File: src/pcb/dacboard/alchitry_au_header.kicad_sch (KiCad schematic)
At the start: 0 parts

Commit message: dacboard routing
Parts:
- added J14, J15, J17, J18, J19, J20, J21, J4, J6: Conn_01x14, Connector_PinHeader_2.54mm:PinHeader_1x14_P2.54mm_Vertical, symbol Connector_Generic:Conn_01x14
- added J22: Conn_01x06, Connector_PinHeader_2.54mm:PinHeader_1x06_P2.54mm_Vertical, symbol Connector_Generic:Conn_01x06
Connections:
- new net AUX_IO1: J20.9 (Pin_9), J22.1 (Pin_1)
- new net AUX_IO2: J20.10 (Pin_10), J22.2 (Pin_2)
- new net AUX_IO3: J20.11 (Pin_11), J22.3 (Pin_3)
- new net AUX_IO4: J20.12 (Pin_12), J22.4 (Pin_4)
- new net AUX_IO5: J20.13 (Pin_13), J22.5 (Pin_5)
- new net AUX_IO6: J20.14 (Pin_14), J22.6 (Pin_6)
- new net CS_N_CH1: J4.4 (Pin_4)
- new net CS_N_CH10: J14.14 (Pin_14)
- new net CS_N_CH11: J15.5 (Pin_5)
- new net CS_N_CH12: J15.9 (Pin_9)
- new net CS_N_CH13: J15.13 (Pin_13)
- new net CS_N_CH14: J17.4 (Pin_4)
- new net CS_N_CH15: J17.8 (Pin_8)
- new net CS_N_CH16: J17.13 (Pin_13)
- new net CS_N_CH17: J18.4 (Pin_4)
- new net CS_N_CH18: J18.8 (Pin_8)
- new net CS_N_CH19: J18.13 (Pin_13)
- new net CS_N_CH2: J4.8 (Pin_8)
- new net CS_N_CH20: J19.4 (Pin_4)
- new net CS_N_CH21: J19.8 (Pin_8)
- new net CS_N_CH22: J19.12 (Pin_12)
- new net CS_N_CH23: J20.3 (Pin_3)
- new net CS_N_CH24: J20.7 (Pin_7)
- new net CS_N_CH3: J4.12 (Pin_12)
- new net CS_N_CH4: J6.3 (Pin_3)
- new net CS_N_CH5: J6.7 (Pin_7)
- new net CS_N_CH6: J6.11 (Pin_11)
- new net CS_N_CH7: J14.2 (Pin_2)
- new net CS_N_CH8: J14.6 (Pin_6)
- new net CS_N_CH9: J14.10 (Pin_10)
- new net LDAC_N_CH1: J4.5 (Pin_5)
- new net LDAC_N_CH10: J15.2 (Pin_2)
- new net LDAC_N_CH11: J15.6 (Pin_6)
- new net LDAC_N_CH12: J15.10 (Pin_10)
- new net LDAC_N_CH13: J15.14 (Pin_14)
- new net LDAC_N_CH14: J17.5 (Pin_5)
- new net LDAC_N_CH15: J17.10 (Pin_10)
- new net LDAC_N_CH16: J17.14 (Pin_14)
- new net LDAC_N_CH17: J18.5 (Pin_5)
- new net LDAC_N_CH18: J18.10 (Pin_10)
- new net LDAC_N_CH19: J18.14 (Pin_14)
- new net LDAC_N_CH2: J4.9 (Pin_9)
- new net LDAC_N_CH20: J19.5 (Pin_5)
- new net LDAC_N_CH21: J19.9 (Pin_9)
- new net LDAC_N_CH22: J19.13 (Pin_13)
- new net LDAC_N_CH23: J20.4 (Pin_4)
- new net LDAC_N_CH24: J20.8 (Pin_8)
- new net LDAC_N_CH3: J4.13 (Pin_13)
- new net LDAC_N_CH4: J6.4 (Pin_4)
- new net LDAC_N_CH5: J6.8 (Pin_8)
- new net LDAC_N_CH6: J6.12 (Pin_12)
- new net LDAC_N_CH7: J14.3 (Pin_3)
- new net LDAC_N_CH8: J14.7 (Pin_7)
- new net LDAC_N_CH9: J14.11 (Pin_11)
- new net MOSI_CH1: J4.3 (Pin_3)
- new net MOSI_CH10: J14.13 (Pin_13)
- new net MOSI_CH11: J15.4 (Pin_4)
- new net MOSI_CH12: J15.8 (Pin_8)
- new net MOSI_CH13: J15.12 (Pin_12)
- new net MOSI_CH14: J17.3 (Pin_3)
- new net MOSI_CH15: J17.7 (Pin_7)
- new net MOSI_CH16: J17.12 (Pin_12)
- new net MOSI_CH17: J18.3 (Pin_3)
- new net MOSI_CH18: J18.7 (Pin_7)
- new net MOSI_CH19: J18.12 (Pin_12)
- new net MOSI_CH2: J4.7 (Pin_7)
- new net MOSI_CH20: J19.3 (Pin_3)
- new net MOSI_CH21: J19.7 (Pin_7)
- new net MOSI_CH22: J19.11 (Pin_11)
- new net MOSI_CH23: J20.2 (Pin_2)
- new net MOSI_CH24: J20.6 (Pin_6)
- new net MOSI_CH3: J4.11 (Pin_11)
- new net MOSI_CH4: J6.2 (Pin_2)
- new net MOSI_CH5: J6.6 (Pin_6)
- new net MOSI_CH6: J6.10 (Pin_10)
- new net MOSI_CH7: J6.14 (Pin_14)
- new net MOSI_CH8: J14.5 (Pin_5)
- new net MOSI_CH9: J14.9 (Pin_9)
- new net NGND: J14.1 (Pin_1), J15.1 (Pin_1), J17.1 (Pin_1), J18.1 (Pin_1), J19.1 (Pin_1), J20.1 (Pin_1), J21.3 (Pin_3), J4.1 (Pin_1), J6.1 (Pin_1)
- new net SCLK_CH1: J4.2 (Pin_2)
- new net SCLK_CH10: J14.12 (Pin_12)
- new net SCLK_CH11: J15.3 (Pin_3)
- new net SCLK_CH12: J15.7 (Pin_7)
- new net SCLK_CH13: J15.11 (Pin_11)
- new net SCLK_CH14: J17.2 (Pin_2)
- new net SCLK_CH15: J17.6 (Pin_6)
- new net SCLK_CH16: J17.11 (Pin_11)
- new net SCLK_CH17: J18.2 (Pin_2)
- new net SCLK_CH18: J18.6 (Pin_6)
- new net SCLK_CH19: J18.11 (Pin_11)
- new net SCLK_CH2: J4.6 (Pin_6)
- new net SCLK_CH20: J19.2 (Pin_2)
- new net SCLK_CH21: J19.6 (Pin_6)
- new net SCLK_CH22: J19.10 (Pin_10)
- new net SCLK_CH23: J19.14 (Pin_14)
- new net SCLK_CH24: J20.5 (Pin_5)
- new net SCLK_CH3: J4.10 (Pin_10)
- new net SCLK_CH4: J4.14 (Pin_14)
- new net SCLK_CH5: J6.5 (Pin_5)
- new net SCLK_CH6: J6.9 (Pin_9)
- new net SCLK_CH7: J6.13 (Pin_13)
- new net SCLK_CH8: J14.4 (Pin_4)
- new net SCLK_CH9: J14.8 (Pin_8)
- new net VCCN: J21.1 (Pin_1), J21.2 (Pin_2)
- no-connect marks 0 -> 13

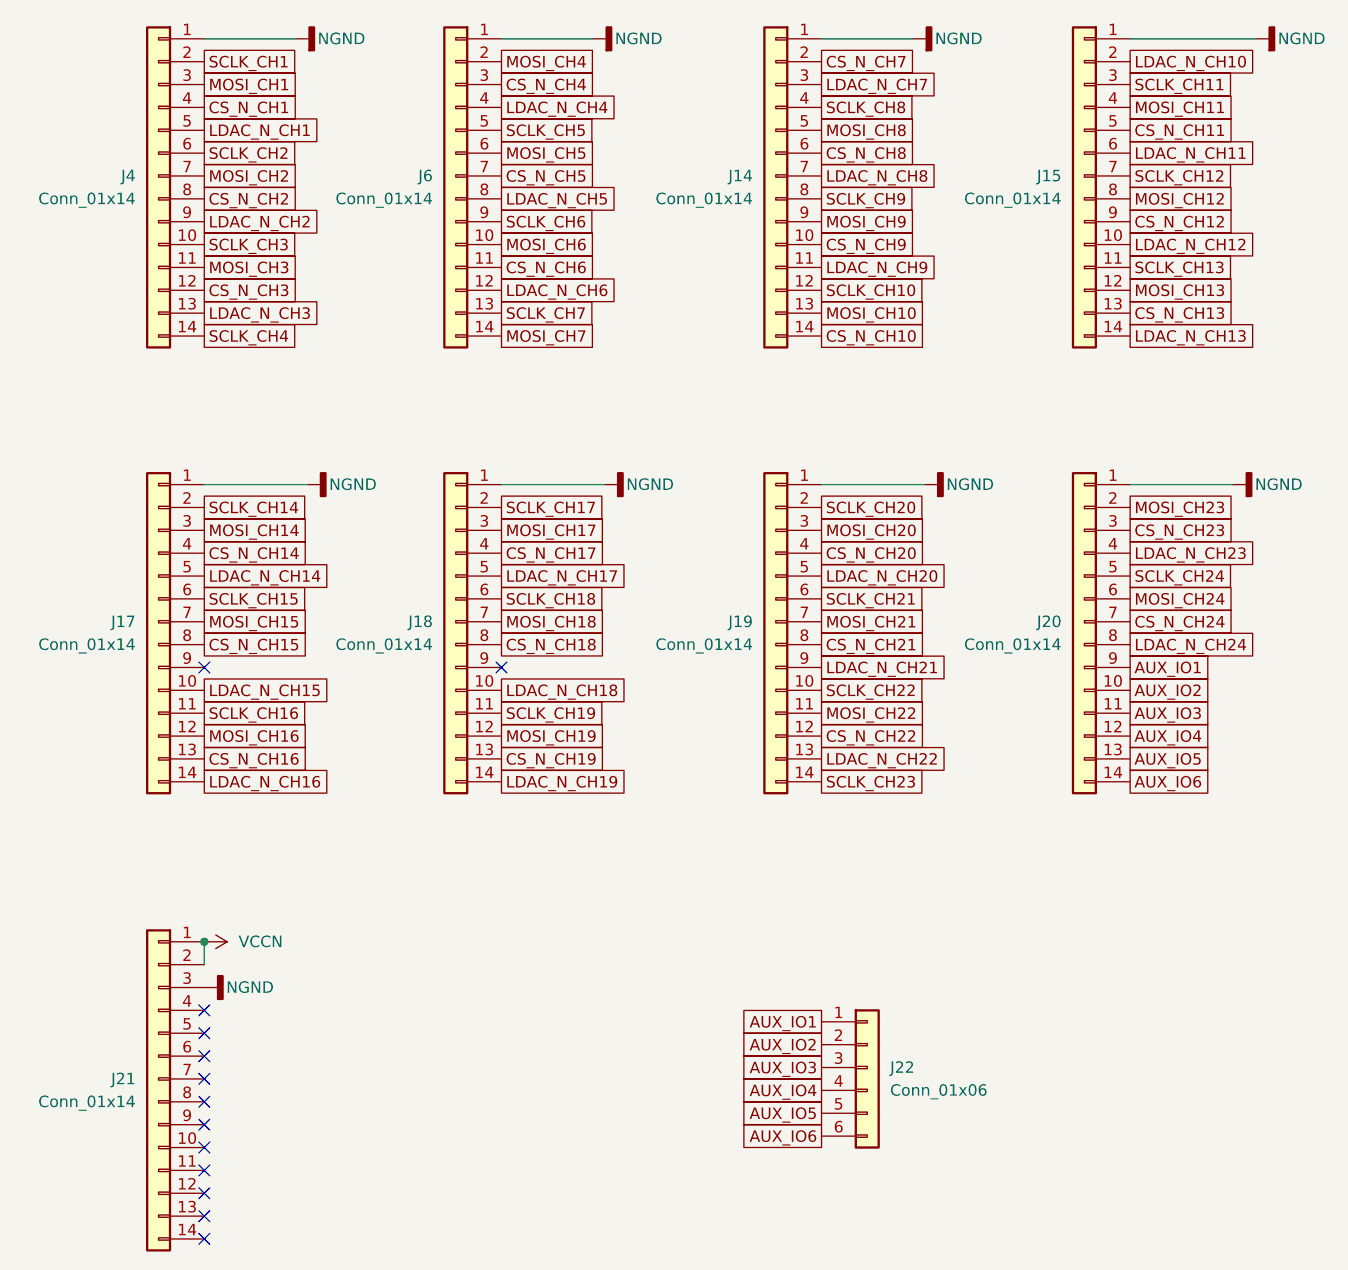
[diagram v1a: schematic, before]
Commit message: finished routing fpga connections
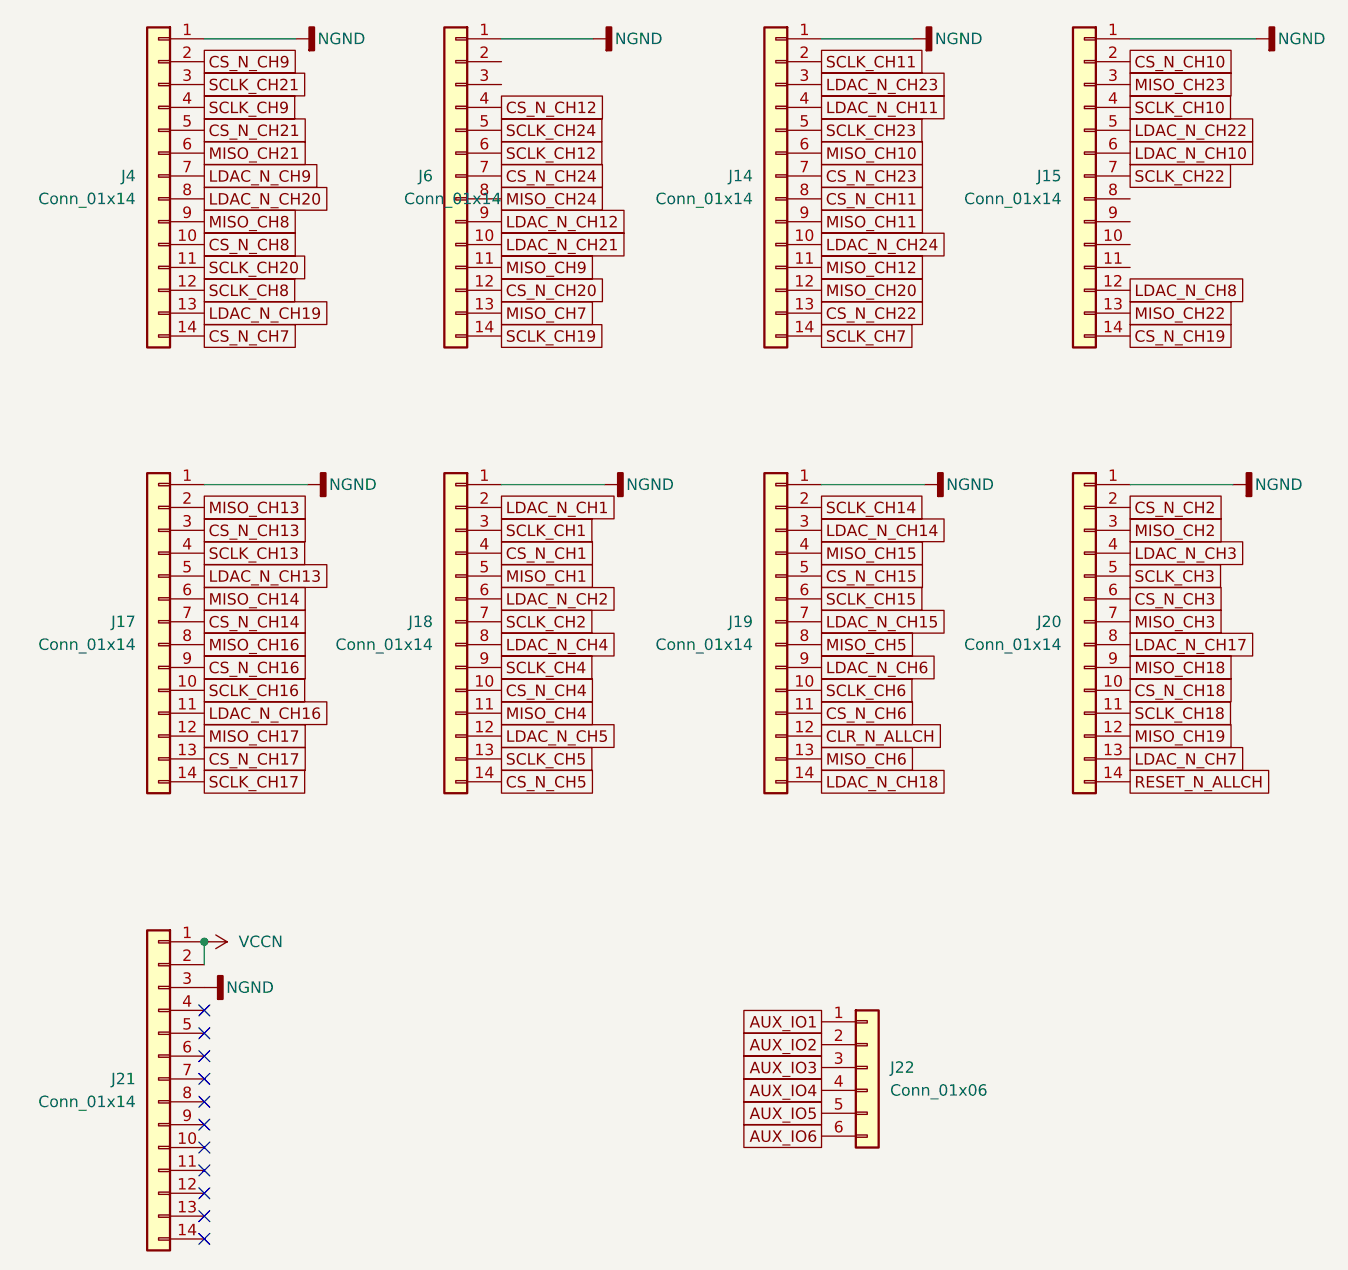
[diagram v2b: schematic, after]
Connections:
- net MOSI_CH1 is gone; now on net SCLK_CH21: J4.3 (Pin_3)
- net MOSI_CH10 is gone; now on net CS_N_CH22: J14.13 (Pin_13)
- net MOSI_CH11 is gone; now on net SCLK_CH10: J15.4 (Pin_4)
- net MOSI_CH13 is gone; now on net LDAC_N_CH8: J15.12 (Pin_12)
- net MOSI_CH14 is gone; now on net CS_N_CH13: J17.3 (Pin_3)
- net MOSI_CH15 is gone; now on net CS_N_CH14: J17.7 (Pin_7)
- net MOSI_CH17 is gone; now on net SCLK_CH1: J18.3 (Pin_3)
- net MOSI_CH18 is gone; now on net SCLK_CH2: J18.7 (Pin_7)
- net MOSI_CH19 is gone; now on net LDAC_N_CH5: J18.12 (Pin_12)
- net MOSI_CH2 is gone; now on net LDAC_N_CH9: J4.7 (Pin_7)
- net MOSI_CH20 is gone; now on net LDAC_N_CH14: J19.3 (Pin_3)
- net MOSI_CH21 is gone; now on net LDAC_N_CH15: J19.7 (Pin_7)
- net MOSI_CH22 is gone; now on net CS_N_CH6: J19.11 (Pin_11)
- net MOSI_CH23 is gone; now on net CS_N_CH2: J20.2 (Pin_2)
- net MOSI_CH24 is gone; now on net CS_N_CH3: J20.6 (Pin_6)
- net MOSI_CH3 is gone; now on net SCLK_CH20: J4.11 (Pin_11)
- net MOSI_CH5 is gone; now on net SCLK_CH12: J6.6 (Pin_6)
- net MOSI_CH6 is gone; now on net LDAC_N_CH21: J6.10 (Pin_10)
- net MOSI_CH7 is gone; now on net SCLK_CH19: J6.14 (Pin_14)
- net MOSI_CH8 is gone; now on net SCLK_CH23: J14.5 (Pin_5)
- net AUX_IO1: no longer J20.9 (Pin_9)
- net AUX_IO2: no longer J20.10 (Pin_10)
- net AUX_IO3: no longer J20.11 (Pin_11)
- net AUX_IO4: no longer J20.12 (Pin_12)
- net AUX_IO5: no longer J20.13 (Pin_13)
- net AUX_IO6: no longer J20.14 (Pin_14)
- net CS_N_CH1: now also J18.4 (Pin_4); no longer J4.4 (Pin_4)
- net CS_N_CH10: now also J15.2 (Pin_2); no longer J14.14 (Pin_14)
- net CS_N_CH11: now also J14.8 (Pin_8); no longer J15.5 (Pin_5)
- net CS_N_CH12: now also J6.4 (Pin_4); no longer J15.9 (Pin_9)
- net CS_N_CH13: no longer J15.13 (Pin_13)
- net CS_N_CH14: no longer J17.4 (Pin_4)
- net CS_N_CH15: now also J19.5 (Pin_5); no longer J17.8 (Pin_8)
- net CS_N_CH16: now also J17.9 (Pin_9); no longer J17.13 (Pin_13)
- net CS_N_CH17: now also J17.13 (Pin_13); no longer J18.4 (Pin_4)
- net CS_N_CH18: now also J20.10 (Pin_10); no longer J18.8 (Pin_8)
- net CS_N_CH19: now also J15.14 (Pin_14); no longer J18.13 (Pin_13)
- net CS_N_CH2: no longer J4.8 (Pin_8)
- net CS_N_CH20: now also J6.12 (Pin_12); no longer J19.4 (Pin_4)
- net CS_N_CH21: now also J4.5 (Pin_5); no longer J19.8 (Pin_8)
- net CS_N_CH22: no longer J19.12 (Pin_12)
- net CS_N_CH23: now also J14.7 (Pin_7); no longer J20.3 (Pin_3)
- net CS_N_CH24: now also J6.7 (Pin_7); no longer J20.7 (Pin_7)
- net CS_N_CH3: no longer J4.12 (Pin_12)
- net CS_N_CH4: now also J18.10 (Pin_10); no longer J6.3 (Pin_3)
- net CS_N_CH5: now also J18.14 (Pin_14); no longer J6.7 (Pin_7)
- net CS_N_CH6: no longer J6.11 (Pin_11)
- net CS_N_CH7: now also J4.14 (Pin_14); no longer J14.2 (Pin_2)
- net CS_N_CH8: now also J4.10 (Pin_10); no longer J14.6 (Pin_6)
- net CS_N_CH9: now also J4.2 (Pin_2); no longer J14.10 (Pin_10)
- net LDAC_N_CH1: now also J18.2 (Pin_2); no longer J4.5 (Pin_5)
- net LDAC_N_CH10: now also J15.6 (Pin_6); no longer J15.2 (Pin_2)
- net LDAC_N_CH11: now also J14.4 (Pin_4); no longer J15.6 (Pin_6)
- net LDAC_N_CH12: now also J6.9 (Pin_9); no longer J15.10 (Pin_10)
- net LDAC_N_CH13: now also J17.5 (Pin_5); no longer J15.14 (Pin_14)
- net LDAC_N_CH14: no longer J17.5 (Pin_5)
- net LDAC_N_CH15: no longer J17.10 (Pin_10)
- net LDAC_N_CH16: now also J17.11 (Pin_11); no longer J17.14 (Pin_14)
- net LDAC_N_CH17: now also J20.8 (Pin_8); no longer J18.5 (Pin_5)
- net LDAC_N_CH18: now also J19.14 (Pin_14); no longer J18.10 (Pin_10)
- net LDAC_N_CH19: now also J4.13 (Pin_13); no longer J18.14 (Pin_14)
- net LDAC_N_CH2: now also J18.6 (Pin_6); no longer J4.9 (Pin_9)
- net LDAC_N_CH20: now also J4.8 (Pin_8); no longer J19.5 (Pin_5)
- net LDAC_N_CH21: no longer J19.9 (Pin_9)
- net LDAC_N_CH22: now also J15.5 (Pin_5); no longer J19.13 (Pin_13)
- net LDAC_N_CH23: now also J14.3 (Pin_3); no longer J20.4 (Pin_4)
- net LDAC_N_CH24: now also J14.10 (Pin_10); no longer J20.8 (Pin_8)
- net LDAC_N_CH3: now also J20.4 (Pin_4); no longer J4.13 (Pin_13)
- net LDAC_N_CH4: now also J18.8 (Pin_8); no longer J6.4 (Pin_4)
- net LDAC_N_CH5: no longer J6.8 (Pin_8)
- net LDAC_N_CH6: now also J19.9 (Pin_9); no longer J6.12 (Pin_12)
- net LDAC_N_CH7: now also J20.13 (Pin_13); no longer J14.3 (Pin_3)
- net LDAC_N_CH8: no longer J14.7 (Pin_7)
- net LDAC_N_CH9: no longer J14.11 (Pin_11)
- net SCLK_CH1: no longer J4.2 (Pin_2)
- net SCLK_CH10: no longer J14.12 (Pin_12)
- net SCLK_CH11: now also J14.2 (Pin_2); no longer J15.3 (Pin_3)
- net SCLK_CH12: no longer J15.7 (Pin_7)
- net SCLK_CH13: now also J17.4 (Pin_4); no longer J15.11 (Pin_11)
- net SCLK_CH14: now also J19.2 (Pin_2); no longer J17.2 (Pin_2)
- net SCLK_CH15: now also J19.6 (Pin_6); no longer J17.6 (Pin_6)
- net SCLK_CH16: now also J17.10 (Pin_10); no longer J17.11 (Pin_11)
- net SCLK_CH17: now also J17.14 (Pin_14); no longer J18.2 (Pin_2)
- net SCLK_CH18: now also J20.11 (Pin_11); no longer J18.6 (Pin_6)
- net SCLK_CH19: no longer J18.11 (Pin_11)
- net SCLK_CH2: no longer J4.6 (Pin_6)
- net SCLK_CH20: no longer J19.2 (Pin_2)
- net SCLK_CH21: no longer J19.6 (Pin_6)
- net SCLK_CH22: now also J15.7 (Pin_7); no longer J19.10 (Pin_10)
- net SCLK_CH23: no longer J19.14 (Pin_14)
- net SCLK_CH24: now also J6.5 (Pin_5); no longer J20.5 (Pin_5)
- net SCLK_CH3: now also J20.5 (Pin_5); no longer J4.10 (Pin_10)
- net SCLK_CH4: now also J18.9 (Pin_9); no longer J4.14 (Pin_14)
- net SCLK_CH5: now also J18.13 (Pin_13); no longer J6.5 (Pin_5)
- net SCLK_CH6: now also J19.10 (Pin_10); no longer J6.9 (Pin_9)
- net SCLK_CH7: now also J14.14 (Pin_14); no longer J6.13 (Pin_13)
- net SCLK_CH8: now also J4.12 (Pin_12); no longer J14.4 (Pin_4)
- net SCLK_CH9: now also J4.4 (Pin_4); no longer J14.8 (Pin_8)
- net MOSI_CH12: no longer names the net of J15.8 (Pin_8)
- net MOSI_CH16 renamed MISO_CH17
- net MOSI_CH4: no longer names the net of J6.2 (Pin_2)
- net MOSI_CH9 renamed MISO_CH11
- new net CLR_N_ALLCH: J19.12 (Pin_12)
- new net MISO_CH1: J18.5 (Pin_5)
- new net MISO_CH10: J14.6 (Pin_6)
- new net MISO_CH12: J14.11 (Pin_11)
- new net MISO_CH13: J17.2 (Pin_2)
- new net MISO_CH14: J17.6 (Pin_6)
- new net MISO_CH15: J19.4 (Pin_4)
- new net MISO_CH16: J17.8 (Pin_8)
- new net MISO_CH18: J20.9 (Pin_9)
- new net MISO_CH19: J20.12 (Pin_12)
- new net MISO_CH2: J20.3 (Pin_3)
- new net MISO_CH20: J14.12 (Pin_12)
- new net MISO_CH21: J4.6 (Pin_6)
- new net MISO_CH22: J15.13 (Pin_13)
- new net MISO_CH23: J15.3 (Pin_3)
- new net MISO_CH24: J6.8 (Pin_8)
- new net MISO_CH3: J20.7 (Pin_7)
- new net MISO_CH4: J18.11 (Pin_11)
- new net MISO_CH5: J19.8 (Pin_8)
- new net MISO_CH6: J19.13 (Pin_13)
- new net MISO_CH7: J6.13 (Pin_13)
- new net MISO_CH8: J4.9 (Pin_9)
- new net MISO_CH9: J6.11 (Pin_11)
- new net RESET_N_ALLCH: J20.14 (Pin_14)
- no-connect marks 13 -> 11
